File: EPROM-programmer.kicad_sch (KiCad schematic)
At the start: 34 parts, among them J1 ZIF-socket, J2 ISP, J3 DAC_A, J4 DAC_B, J5 GND, P1 USB-C, SW1 SW_Push, U1 ATmega1284-P, U2 MCP2221AxP, U3 MCP4812, Y1 20M

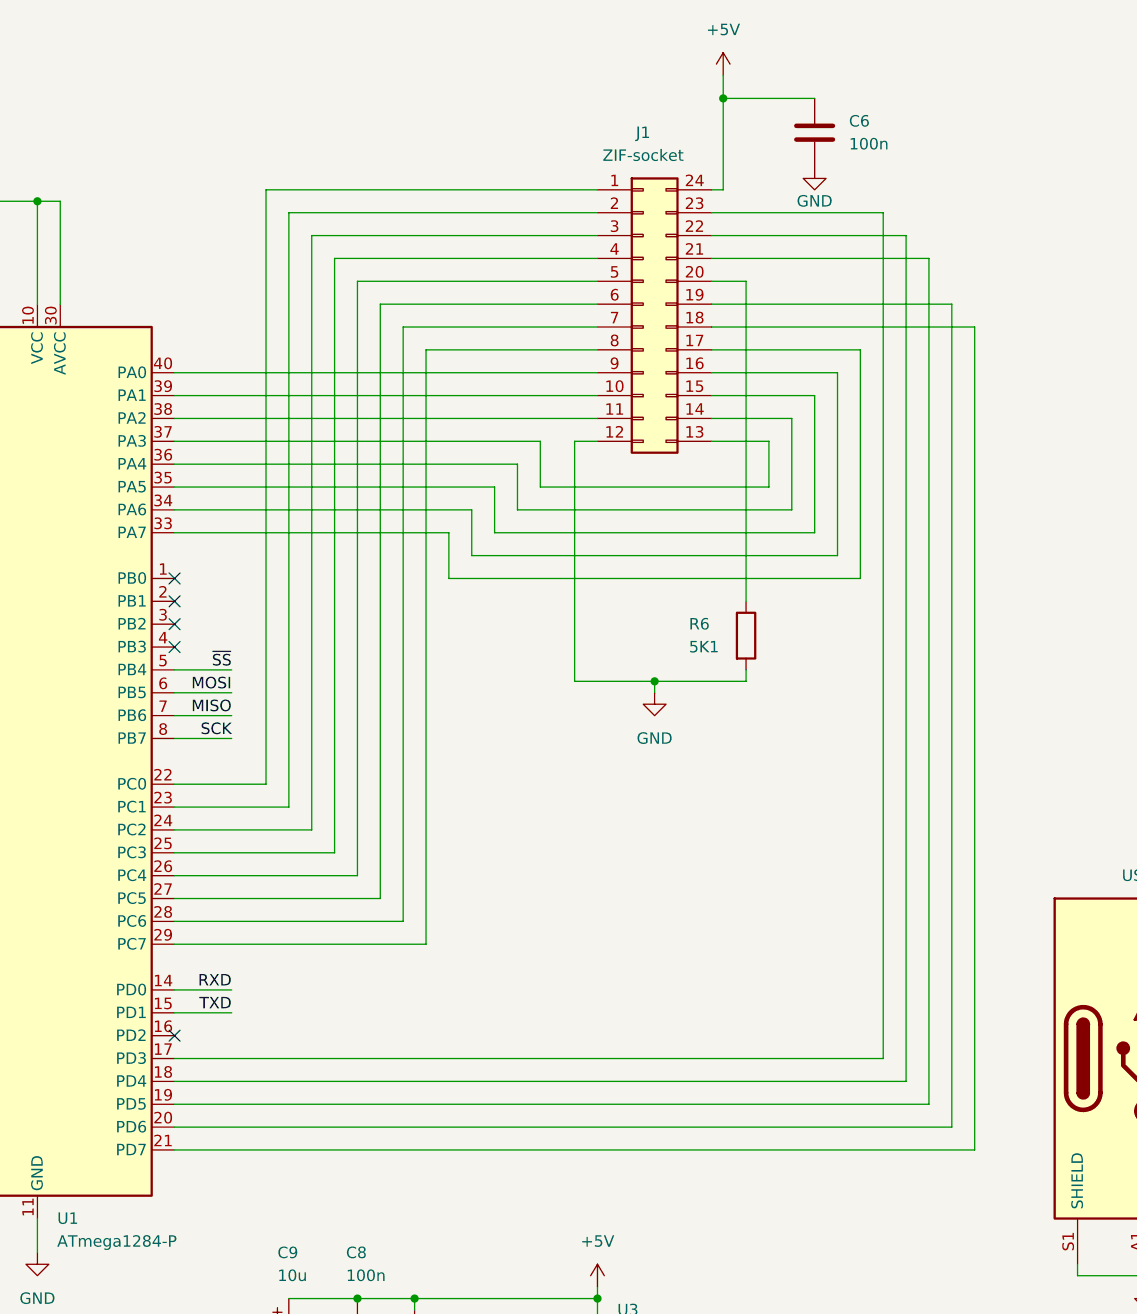
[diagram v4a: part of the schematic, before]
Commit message: Update connections to ZIF-socket
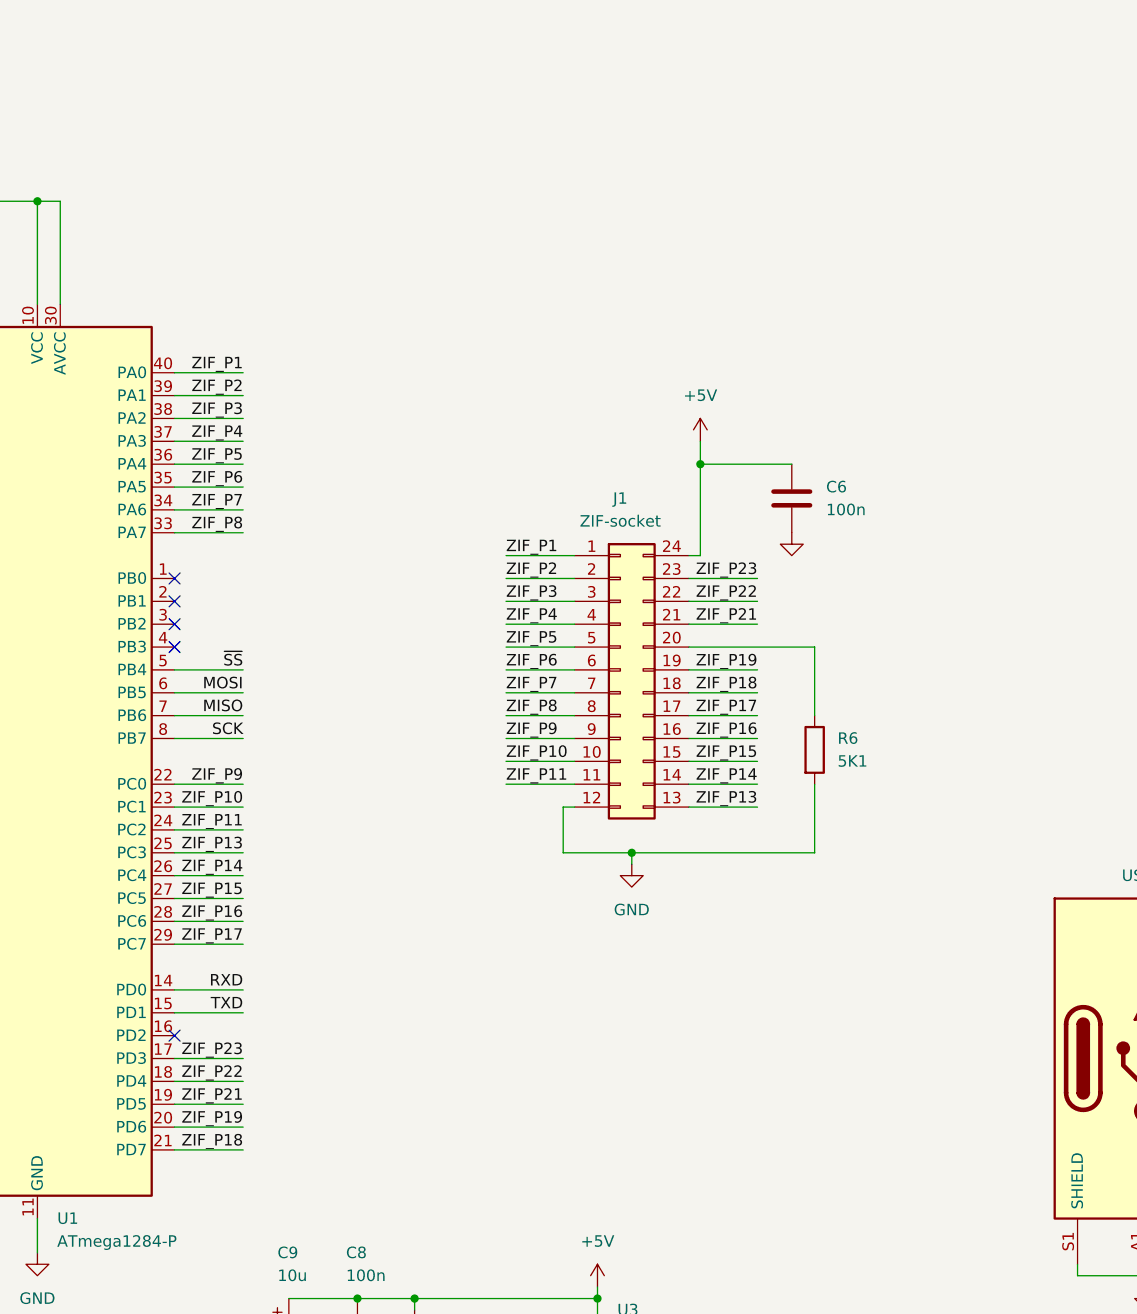
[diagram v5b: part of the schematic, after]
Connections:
- net ZIF_P1: now reaches J1.1 (Pin_1)
- net ZIF_P1: now also U1.40 (PA0); no longer U1.22 (PC0)
- net ZIF_P10: now reaches J1.10 (Pin_10)
- net ZIF_P10: now also U1.23 (PC1); no longer U1.39 (PA1)
- net ZIF_P11: now reaches J1.11 (Pin_11)
- net ZIF_P11: now also U1.24 (PC2); no longer U1.38 (PA2)
- net ZIF_P13: now reaches J1.13 (Pin_13)
- net ZIF_P13: now also U1.25 (PC3); no longer U1.37 (PA3)
- net ZIF_P14: now reaches J1.14 (Pin_14)
- net ZIF_P14: now also U1.26 (PC4); no longer U1.36 (PA4)
- net ZIF_P15: now reaches J1.15 (Pin_15)
- net ZIF_P15: now also U1.27 (PC5); no longer U1.35 (PA5)
- net ZIF_P16: now reaches J1.16 (Pin_16)
- net ZIF_P16: now also U1.28 (PC6); no longer U1.34 (PA6)
- net ZIF_P17: now reaches J1.17 (Pin_17)
- net ZIF_P17: now also U1.29 (PC7); no longer U1.33 (PA7)
- net ZIF_P18: now reaches J1.18 (Pin_18), U1.21 (PD7)
- net ZIF_P19: now reaches J1.19 (Pin_19), U1.20 (PD6)
- net ZIF_P2: now reaches J1.2 (Pin_2)
- net ZIF_P2: now also U1.39 (PA1); no longer U1.23 (PC1)
- net ZIF_P21: now reaches J1.21 (Pin_21), U1.19 (PD5)
- net ZIF_P22: now reaches J1.22 (Pin_22), U1.18 (PD4)
- net ZIF_P23: now reaches J1.23 (Pin_23), U1.17 (PD3)
- net ZIF_P3: now reaches J1.3 (Pin_3)
- net ZIF_P3: now also U1.38 (PA2); no longer U1.24 (PC2)
- net ZIF_P4: now reaches J1.4 (Pin_4)
- net ZIF_P4: now also U1.37 (PA3); no longer U1.25 (PC3)
- net ZIF_P5: now reaches J1.5 (Pin_5)
- net ZIF_P5: now also U1.36 (PA4); no longer U1.26 (PC4)
- net ZIF_P6: now reaches J1.6 (Pin_6)
- net ZIF_P6: now also U1.35 (PA5); no longer U1.27 (PC5)
- net ZIF_P7: now reaches J1.7 (Pin_7)
- net ZIF_P7: now also U1.34 (PA6); no longer U1.28 (PC6)
- net ZIF_P8: now reaches J1.8 (Pin_8)
- net ZIF_P8: now also U1.33 (PA7); no longer U1.29 (PC7)
- net ZIF_P9: now reaches J1.9 (Pin_9)
- net ZIF_P9: now also U1.22 (PC0); no longer U1.40 (PA0)
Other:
- moved on the sheet: C6, J1, R6

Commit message: Fix capacitor-stuff
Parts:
- added C10: 100n, Capacitor_THT:C_Rect_L4.6mm_W3.0mm_P2.50mm_MKS02_FKP02, symbol Device:C
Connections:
- net +5V: now also C10.1
- net GND: now also C10.2
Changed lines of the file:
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@@
   (junction (at 99.06 157.48) (diameter 0) (color 0 0 0 0)
   )
+  (junction (at 25.4 35.56) (diameter 0) (color 0 0 0 0)
+  )
   (junction (at 180.34 154.94) (diameter 0) (color 0 0 0 0)
   )
@@
   )
   (junction (at 195.58 121.92) (diameter 0) (color 0 0 0 0)
+  )
+  (junction (at 21.59 43.18) (diameter 0) (color 0 0 0 0)
   )
   (junction (at 233.68 106.68) (diameter 0) (color 0 0 0 0)
@@
     (stroke (width 0) (type default))
   )
+  (wire (pts (xy 21.59 43.18) (xy 25.4 43.18))
+    (stroke (width 0) (type default))
+  )
   (wire (pts (xy 72.39 72.39) (xy 80.01 72.39))
     (stroke (width 0) (type default))
@@
     (stroke (width 0) (type default))
   )
-  (wire (pts (xy 17.78 35.56) (xy 33.02 35.56))
+  (wire (pts (xy 17.78 35.56) (xy 25.4 35.56))
     (stroke (width 0) (type default))
   )
@@
     (stroke (width 0) (type default))
   )
+  (wire (pts (xy 17.78 43.18) (xy 21.59 43.18))
+    (stroke (width 0) (type default))
+  )
   (wire (pts (xy 195.58 121.92) (xy 215.9 121.92))
     (stroke (width 0) (type default))
@@
     (stroke (width 0) (type default))
   )
+  (wire (pts (xy 25.4 35.56) (xy 33.02 35.56))
+    (stroke (width 0) (type default))
+  )
   (wire (pts (xy 132.08 176.53) (xy 143.51 176.53))
     (stroke (width 0) (type default))
@@
   )
   (symbol (lib_id "Device:C") (at 17.78 39.37 0) (unit 1)
-    (in_bom yes) (on_board yes) (dnp no) (fields_autoplaced)
-    (property "Reference" "C4" (at 21.59 38.1 0)
-      (effects (font (size 1.27 1.27)) (justify left))
-    )
-    (property "Value" "100n" (at 21.59 40.64 0)
+    (in_bom yes) (on_board yes) (dnp no)
+    (property "Reference" "C4" (at 16.51 30.48 0)
+      (effects (font (size 1.27 1.27)) (justify left))
+    )
+    (property "Value" "100n" (at 16.51 33.02 0)
       (effects (font (size 1.27 1.27)) (justify left))
     )
@@
     )
   )
-  (symbol (lib_id "power:GND") (at 17.78 43.18 0) (unit 1)
-    (in_bom yes) (on_board yes) (dnp no) (fields_autoplaced)
-    (property "Reference" "#PWR015" (at 17.78 49.53 0)
-      (effects (font (size 1.27 1.27)) hide)
-    )
-    (property "Value" "GND" (at 17.78 48.26 0)
-      (effects (font (size 1.27 1.27)))
-    )
-    (property "Footprint" "" (at 17.78 43.18 0)
-      (effects (font (size 1.27 1.27)) hide)
-    )
-    (property "Datasheet" "" (at 17.78 43.18 0)
+  (symbol (lib_id "power:GND") (at 21.59 43.18 0) (unit 1)
+    (in_bom yes) (on_board yes) (dnp no) (fields_autoplaced)
+    (property "Reference" "#PWR015" (at 21.59 49.53 0)
+      (effects (font (size 1.27 1.27)) hide)
+    )
+    (property "Value" "GND" (at 21.59 48.26 0)
+      (effects (font (size 1.27 1.27)))
+    )
+    (property "Footprint" "" (at 21.59 43.18 0)
+      (effects (font (size 1.27 1.27)) hide)
+    )
+    (property "Datasheet" "" (at 21.59 43.18 0)
       (effects (font (size 1.27 1.27)) hide)
     )
@@
   )
   (symbol (lib_id "Switch:SW_Push") (at 24.13 54.61 0) (unit 1)
-    (in_bom yes) (on_board yes) (dnp no) (fields_autoplaced)
-    (property "Reference" "SW1" (at 24.13 46.99 0)
-      (effects (font (size 1.27 1.27)))
-    )
-    (property "Value" "SW_Push" (at 24.13 49.53 0)
+    (in_bom yes) (on_board yes) (dnp no)
+    (property "Reference" "SW1" (at 16.51 50.8 0)
+      (effects (font (size 1.27 1.27)))
+    )
+    (property "Value" "SW_Push" (at 16.51 53.34 0)
       (effects (font (size 1.27 1.27)))
     )
@@
         )
       )
+    )
+  )
+  (symbol (lib_id "Device:C") (at 25.4 39.37 0) (unit 1)
+    (in_bom yes) (on_board yes) (dnp no)
+    (property "Reference" "C10" (at 24.13 30.48 0)
+      (effects (font (size 1.27 1.27)) (justify left))
+    )
+    (property "Value" "100n" (at 24.13 33.02 0)
+      (effects (font (size 1.27 1.27)) (justify left))
+    )
+    (property "Footprint" "Capacitor_THT:C_Rect_L4.6mm_W3.0mm_P2.50mm_MKS02_FKP02" (at 26.3652 43.18 0)
+      (effects (font (size 1.27 1.27)) hide)
+    )
+    (property "Datasheet" "~" (at 25.4 39.37 0)
+      (effects (font (size 1.27 1.27)) hide)
+    )
+    (pin "1")
+    (pin "2")
+    (instances
+      (project "EPROM-programmer"
+        (path "/8c5576b1-cb3e-4456-837b-2f47818a03ab"
+          (reference "C10") (unit 1)
+        )
+      )

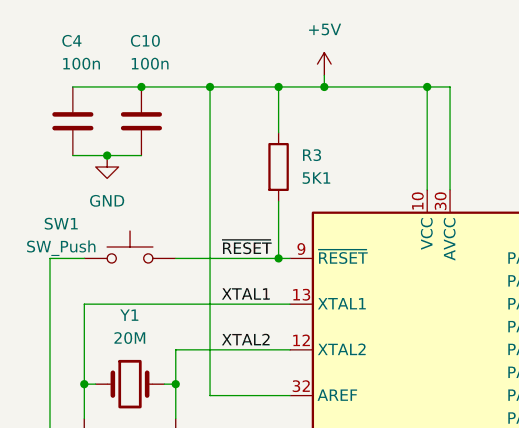
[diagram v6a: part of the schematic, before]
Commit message: Revert "Fix capacitor-stuff"
This reverts commit 9b25b860817774e3e25b1a31baa03ad3e26370b1.
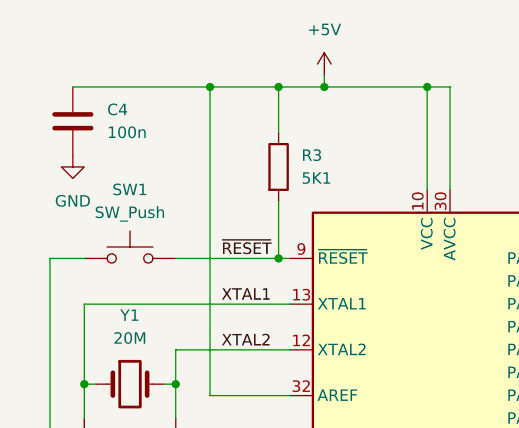
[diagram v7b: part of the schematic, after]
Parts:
- removed C10: 100n, Capacitor_THT:C_Rect_L4.6mm_W3.0mm_P2.50mm_MKS02_FKP02, symbol Device:C
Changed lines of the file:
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@@
   (junction (at 99.06 157.48) (diameter 0) (color 0 0 0 0)
   )
-  (junction (at 25.4 35.56) (diameter 0) (color 0 0 0 0)
-  )
   (junction (at 180.34 154.94) (diameter 0) (color 0 0 0 0)
   )
@@
   )
   (junction (at 195.58 121.92) (diameter 0) (color 0 0 0 0)
-  )
-  (junction (at 21.59 43.18) (diameter 0) (color 0 0 0 0)
   )
   (junction (at 233.68 106.68) (diameter 0) (color 0 0 0 0)
@@
     (stroke (width 0) (type default))
   )
-  (wire (pts (xy 21.59 43.18) (xy 25.4 43.18))
-    (stroke (width 0) (type default))
-  )
   (wire (pts (xy 72.39 72.39) (xy 80.01 72.39))
     (stroke (width 0) (type default))
@@
     (stroke (width 0) (type default))
   )
-  (wire (pts (xy 17.78 35.56) (xy 25.4 35.56))
+  (wire (pts (xy 17.78 35.56) (xy 33.02 35.56))
     (stroke (width 0) (type default))
   )
@@
     (stroke (width 0) (type default))
   )
-  (wire (pts (xy 17.78 43.18) (xy 21.59 43.18))
-    (stroke (width 0) (type default))
-  )
   (wire (pts (xy 195.58 121.92) (xy 215.9 121.92))
     (stroke (width 0) (type default))
@@
     (stroke (width 0) (type default))
   )
-  (wire (pts (xy 25.4 35.56) (xy 33.02 35.56))
-    (stroke (width 0) (type default))
-  )
   (wire (pts (xy 132.08 176.53) (xy 143.51 176.53))
     (stroke (width 0) (type default))
@@
   )
   (symbol (lib_id "Device:C") (at 17.78 39.37 0) (unit 1)
-    (in_bom yes) (on_board yes) (dnp no)
-    (property "Reference" "C4" (at 16.51 30.48 0)
-      (effects (font (size 1.27 1.27)) (justify left))
-    )
-    (property "Value" "100n" (at 16.51 33.02 0)
+    (in_bom yes) (on_board yes) (dnp no) (fields_autoplaced)
+    (property "Reference" "C4" (at 21.59 38.1 0)
+      (effects (font (size 1.27 1.27)) (justify left))
+    )
+    (property "Value" "100n" (at 21.59 40.64 0)
       (effects (font (size 1.27 1.27)) (justify left))
     )
@@
     )
   )
-  (symbol (lib_id "power:GND") (at 21.59 43.18 0) (unit 1)
-    (in_bom yes) (on_board yes) (dnp no) (fields_autoplaced)
-    (property "Reference" "#PWR015" (at 21.59 49.53 0)
-      (effects (font (size 1.27 1.27)) hide)
-    )
-    (property "Value" "GND" (at 21.59 48.26 0)
-      (effects (font (size 1.27 1.27)))
-    )
-    (property "Footprint" "" (at 21.59 43.18 0)
-      (effects (font (size 1.27 1.27)) hide)
-    )
-    (property "Datasheet" "" (at 21.59 43.18 0)
+  (symbol (lib_id "power:GND") (at 17.78 43.18 0) (unit 1)
+    (in_bom yes) (on_board yes) (dnp no) (fields_autoplaced)
+    (property "Reference" "#PWR015" (at 17.78 49.53 0)
+      (effects (font (size 1.27 1.27)) hide)
+    )
+    (property "Value" "GND" (at 17.78 48.26 0)
+      (effects (font (size 1.27 1.27)))
+    )
+    (property "Footprint" "" (at 17.78 43.18 0)
+      (effects (font (size 1.27 1.27)) hide)
+    )
+    (property "Datasheet" "" (at 17.78 43.18 0)
       (effects (font (size 1.27 1.27)) hide)
     )
@@
   )
   (symbol (lib_id "Switch:SW_Push") (at 24.13 54.61 0) (unit 1)
-    (in_bom yes) (on_board yes) (dnp no)
-    (property "Reference" "SW1" (at 16.51 50.8 0)
-      (effects (font (size 1.27 1.27)))
-    )
-    (property "Value" "SW_Push" (at 16.51 53.34 0)
+    (in_bom yes) (on_board yes) (dnp no) (fields_autoplaced)
+    (property "Reference" "SW1" (at 24.13 46.99 0)
+      (effects (font (size 1.27 1.27)))
+    )
+    (property "Value" "SW_Push" (at 24.13 49.53 0)
       (effects (font (size 1.27 1.27)))
     )
@@
         )
       )
-    )
-  )
-  (symbol (lib_id "Device:C") (at 25.4 39.37 0) (unit 1)
-    (in_bom yes) (on_board yes) (dnp no)
-    (property "Reference" "C10" (at 24.13 30.48 0)
-      (effects (font (size 1.27 1.27)) (justify left))
-    )
-    (property "Value" "100n" (at 24.13 33.02 0)
-      (effects (font (size 1.27 1.27)) (justify left))
-    )
-    (property "Footprint" "Capacitor_THT:C_Rect_L4.6mm_W3.0mm_P2.50mm_MKS02_FKP02" (at 26.3652 43.18 0)
-      (effects (font (size 1.27 1.27)) hide)
-    )
-    (property "Datasheet" "~" (at 25.4 39.37 0)
-      (effects (font (size 1.27 1.27)) hide)
-    )
-    (pin "1")
-    (pin "2")
-    (instances
-      (project "EPROM-programmer"
-        (path "/8c5576b1-cb3e-4456-837b-2f47818a03ab"
-          (reference "C10") (unit 1)
-        )
-      )
